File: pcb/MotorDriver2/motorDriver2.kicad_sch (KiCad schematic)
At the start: 22 parts, among them Q1 IRLZ44NSTRLPBF, Q6 IRLZ44NSTRLPBF, Q7 IRLZ44NSTRLPBF, Q8 IRLZ44NSTRLPBF

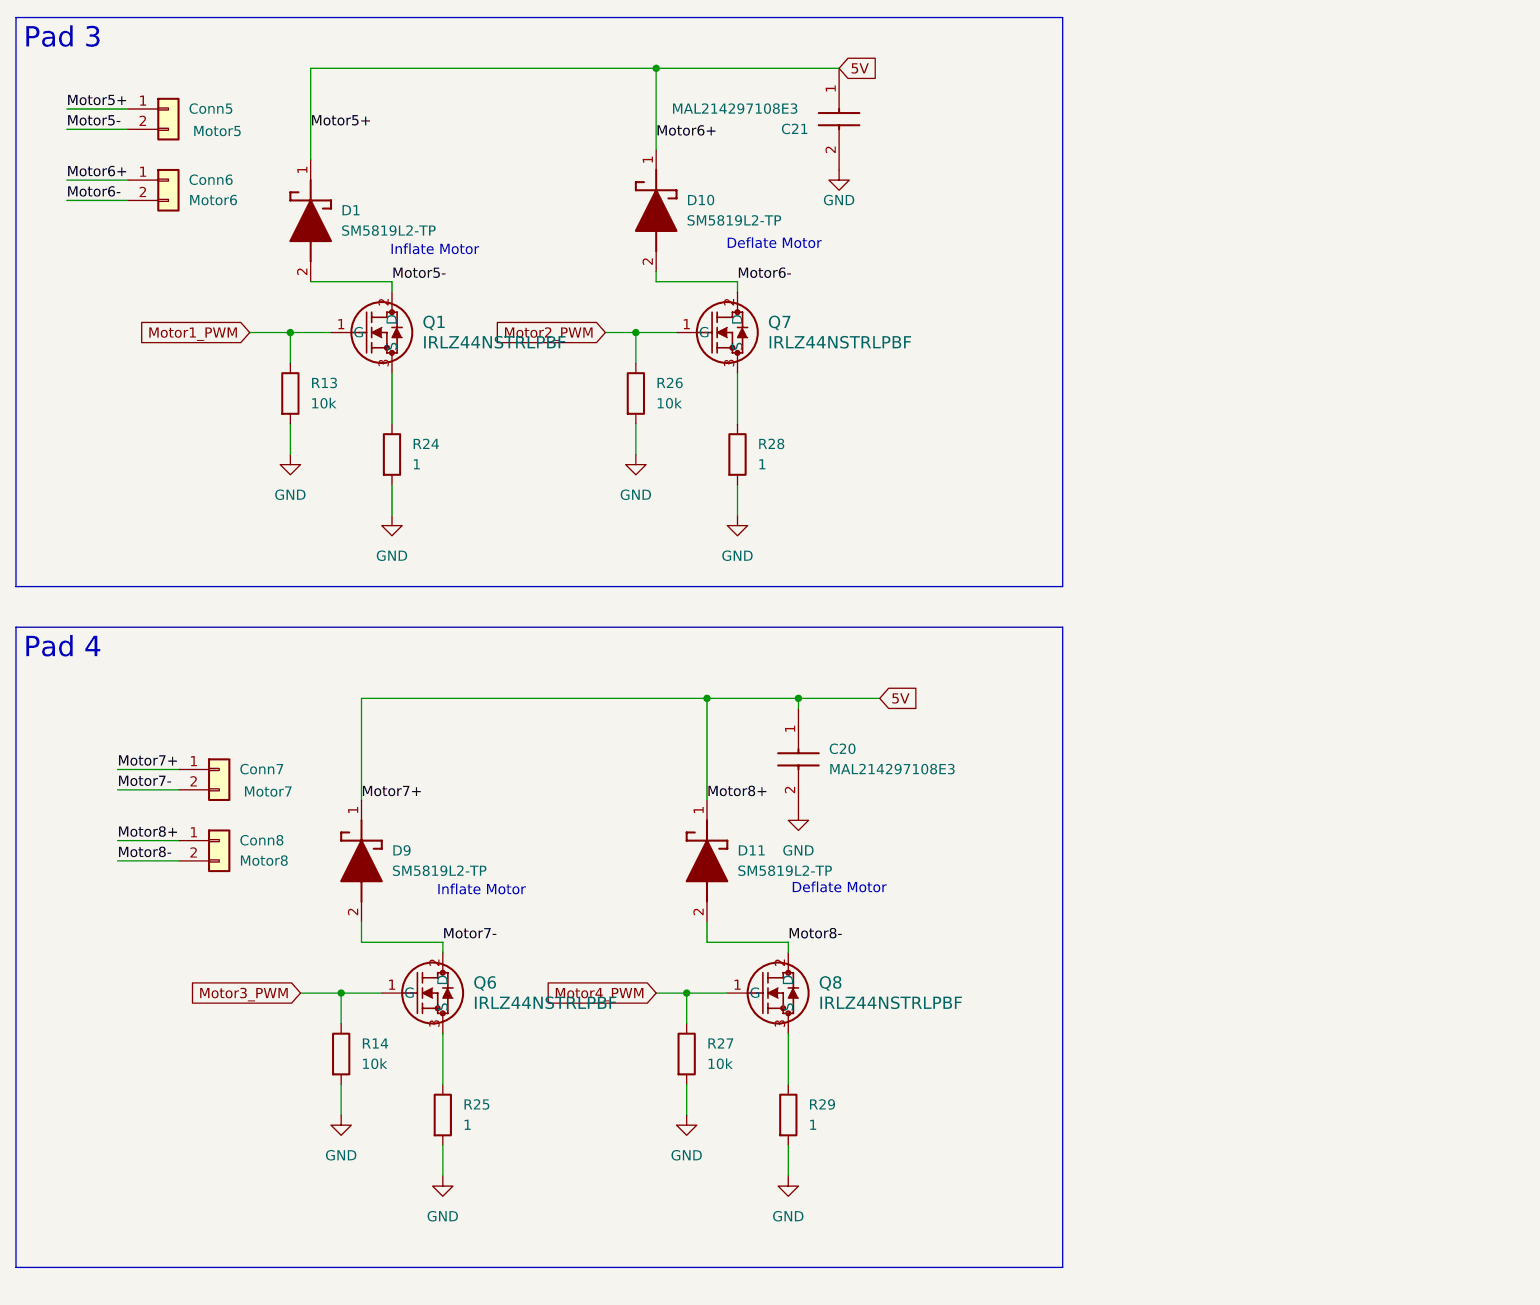
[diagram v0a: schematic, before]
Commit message: Modifying usb uart schematic
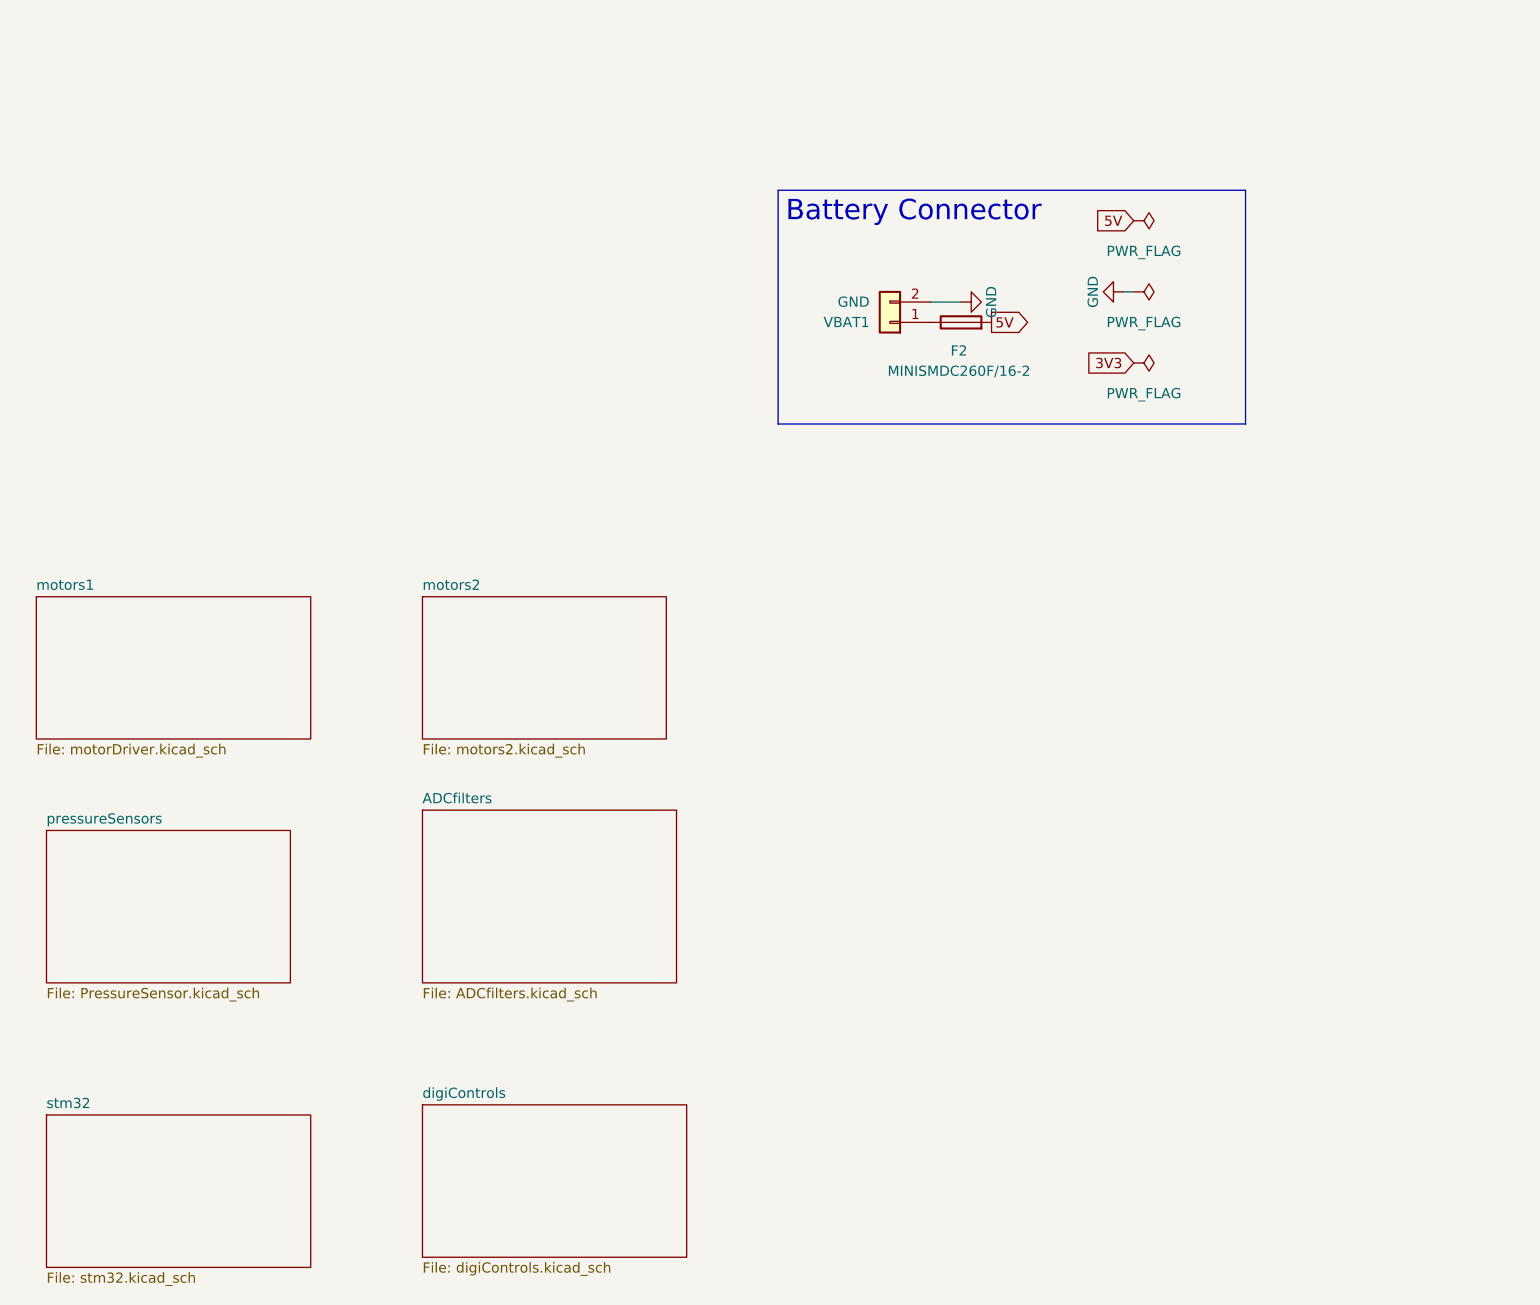
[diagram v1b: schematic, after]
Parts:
- removed C20, C21: MAL214297108E3, footprintLib:CAPAE680X800N, symbol pcb:MAL214297108E3
- removed Conn5: Motor5, Connector_PinHeader_2.54mm:PinHeader_1x02_P2.54mm_Vertical, symbol Connector_Generic:Conn_01x02
- removed Conn6: Motor6, Connector_PinHeader_2.54mm:PinHeader_1x02_P2.54mm_Vertical, symbol Connector_Generic:Conn_01x02
- removed Conn7: Motor7, Connector_PinHeader_2.54mm:PinHeader_1x02_P2.54mm_Vertical, symbol Connector_Generic:Conn_01x02
- removed Conn8: Motor8, Connector_PinHeader_2.54mm:PinHeader_1x02_P2.54mm_Vertical, symbol Connector_Generic:Conn_01x02
- removed D1, D10, D11, D9: SM5819L2-TP, footprintLib:SDO_SM5819L2-TP_MCE, symbol pcb:SM5819L2-TP
- removed Q1, Q6, Q7, Q8: IRLZ44NSTRLPBF, footprintLib:NMOSGDS_D2PAK_INF, symbol pcb:IRLZ44NSTRLPBF
- removed R13, R14, R26, R27: 10k, Resistor_SMD:R_0402_1005Metric, symbol Device:R
- removed R24, R25, R28, R29: 1, Resistor_SMD:R_1206_3216Metric, symbol Device:R
- added F2: MINISMDC260F/16-2, Fuse:Fuse_1812_4532Metric, symbol Device:Fuse
- added VBAT1: GND, Connector_PinHeader_2.54mm:PinHeader_1x02_P2.54mm_Vertical, symbol Connector_Generic:Conn_01x02
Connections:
- net 5V: now also F2.2
- net GND: now also VBAT1.2 (Pin_2)
- new net: F2.1, VBAT1.1 (Pin_1)
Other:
- added sheet ADCfilters (ADCfilters.kicad_sch)
- added sheet digiControls (digiControls.kicad_sch)
- added sheet motors1 (motorDriver.kicad_sch)
- added sheet motors2 (motors2.kicad_sch)
- added sheet pressureSensors (PressureSensor.kicad_sch)
- added sheet stm32 (stm32.kicad_sch)
- note removed: "Deflate Motor"
- note removed: "Inflate Motor"

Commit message: added ideal diode protection
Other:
- moved on the sheet: F2, VBAT1
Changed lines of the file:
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@@
 	(text_box "Battery Connector"
 		(exclude_from_sim no)
-		(at 124.46 48.26 0)
+		(at 130.81 101.6 0)
 		(size 58.42 29.21)
 		(margins 0.9525 0.9525 0.9525 0.9525)
@@
 	(wire
 		(pts
-			(xy 147.32 62.23) (xy 143.51 62.23)
+			(xy 153.67 115.57) (xy 149.86 115.57)
 		)
 		(stroke
@@
 	(wire
 		(pts
-			(xy 167.64 60.96) (xy 168.91 60.96)
+			(xy 173.99 114.3) (xy 175.26 114.3)
 		)
 		(stroke
@@
 	(global_label "5V"
 		(shape input)
-		(at 168.91 52.07 180)
+		(at 175.26 105.41 180)
 		(fields_autoplaced yes)
 		(effects
@@
 		)
 		(property "Intersheetrefs" "${INTERSHEET_REFS}"
-			(at 163.6267 52.07 0)
+			(at 169.9767 105.41 0)
 			(effects
 				(font
@@
 	(global_label "3V3"
 		(shape input)
-		(at 168.91 69.85 180)
+		(at 175.26 123.19 180)
 		(fields_autoplaced yes)
 		(effects
@@
 		)
 		(property "Intersheetrefs" "${INTERSHEET_REFS}"
-			(at 162.4172 69.85 0)
+			(at 168.7672 123.19 0)
 			(effects
 				(font
@@
 	(global_label "5V"
 		(shape output)
-		(at 151.13 64.77 0)
+		(at 157.48 118.11 0)
 		(fields_autoplaced yes)
 		(effects
@@
 		)
 		(property "Intersheetrefs" "${INTERSHEET_REFS}"
-			(at 156.4133 64.77 0)
+			(at 162.7633 118.11 0)
 			(effects
 				(font
@@
 	(symbol
 		(lib_id "power:GND")
-		(at 167.64 60.96 270)
+		(at 173.99 114.3 270)
 		(unit 1)
 		(exclude_from_sim no)
@@
 		(dnp no)
 		(property "Reference" "#PWR012"
-			(at 161.29 60.96 0)
+			(at 167.64 114.3 0)
 			(effects
 				(font
@@
 		)
 		(property "Value" "GND"
-			(at 163.83 60.96 0)
+			(at 170.18 114.3 0)
 			(effects
 				(font
@@
 		)
 		(property "Footprint" ""
-			(at 167.64 60.96 0)
+			(at 173.99 114.3 0)
 			(effects
 				(font
@@
 		)
 		(property "Datasheet" ""
-			(at 167.64 60.96 0)
+			(at 173.99 114.3 0)
 			(effects
 				(font
@@
 		)
 		(property "Description" "Power symbol creates a global label with name \"GND\" , ground"
-			(at 167.64 60.96 0)
+			(at 173.99 114.3 0)
 			(effects
 				(font
@@
 	(symbol
 		(lib_id "power:PWR_FLAG")
-		(at 168.91 52.07 270)
+		(at 175.26 105.41 270)
 		(unit 1)
 		(exclude_from_sim no)
@@
 		(fields_autoplaced yes)
 		(property "Reference" "#FLG01"
-			(at 170.815 52.07 0)
+			(at 177.165 105.41 0)
 			(effects
 				(font
@@
 		)
 		(property "Value" "PWR_FLAG"
-			(at 170.18 55.88 90)
+			(at 176.53 109.22 90)
 			(effects
 				(font
@@
 		)
 		(property "Footprint" ""
-			(at 168.91 52.07 0)
+			(at 175.26 105.41 0)
 			(effects
 				(font
@@
 		)
 		(property "Datasheet" "~"
-			(at 168.91 52.07 0)
+			(at 175.26 105.41 0)
 			(effects
 				(font
@@
 		)
 		(property "Description" "Special symbol for telling ERC where power comes from"
-			(at 168.91 52.07 0)
+			(at 175.26 105.41 0)
 			(effects
 				(font
@@
 	(symbol
 		(lib_id "Connector_Generic:Conn_01x02")
-		(at 138.43 64.77 180)
+		(at 144.78 118.11 180)
 		(unit 1)
 		(exclude_from_sim no)
@@
 		(dnp no)
 		(property "Reference" "VBAT1"
-			(at 135.89 64.77 0)
+			(at 142.24 118.11 0)
 			(effects
 				(font
@@
 		)
 		(property "Value" "GND"
-			(at 135.89 62.2301 0)
+			(at 142.24 115.5701 0)
 			(effects
 				(font
@@
 		)
 		(property "Footprint" "Connector_PinHeader_2.54mm:PinHeader_1x02_P2.54mm_Vertical"
-			(at 138.43 64.77 0)
+			(at 144.78 118.11 0)
 			(effects
 				(font
@@
 		)
 		(property "Datasheet" "~"
-			(at 138.43 64.77 0)
+			(at 144.78 118.11 0)
 			(effects
 				(font
@@
 		)
 		(property "Description" "Generic connector, single row, 01x02, script generated (kicad-library-utils/schlib/autogen/connector/)"
-			(at 138.43 64.77 0)
+			(at 144.78 118.11 0)
 			(effects
 				(font
@@
 	(symbol
 		(lib_id "power:GND")
-		(at 147.32 62.23 90)
+		(at 153.67 115.57 90)
 		(unit 1)
 		(exclude_from_sim no)
@@
 		(dnp no)
 		(property "Reference" "#PWR011"
-			(at 153.67 62.23 0)
+			(at 160.02 115.57 0)
 			(effects
 				(font
@@
 		)
 		(property "Value" "GND"
-			(at 151.13 62.23 0)
+			(at 157.48 115.57 0)
 			(effects
 				(font
@@
 		)
 		(property "Footprint" ""
-			(at 147.32 62.23 0)
+			(at 153.67 115.57 0)
 			(effects
 				(font
@@
 		)
 		(property "Datasheet" ""
-			(at 147.32 62.23 0)
+			(at 153.67 115.57 0)
 			(effects
 				(font
@@
 		)
 		(property "Description" "Power symbol creates a global label with name \"GND\" , ground"
-			(at 147.32 62.23 0)
+			(at 153.67 115.57 0)
 			(effects
 				(font
@@
 	(symbol
 		(lib_id "power:PWR_FLAG")
-		(at 168.91 69.85 270)
+		(at 175.26 123.19 270)
 		(unit 1)
 		(exclude_from_sim no)
@@
 		(fields_autoplaced yes)
 		(property "Reference" "#FLG03"
-			(at 170.815 69.85 0)
+			(at 177.165 123.19 0)
 			(effects
 				(font
@@
 		)
 		(property "Value" "PWR_FLAG"
-			(at 170.18 73.66 90)
+			(at 176.53 127 90)
 			(effects
 				(font
@@
 		)
 		(property "Footprint" ""
-			(at 168.91 69.85 0)
+			(at 175.26 123.19 0)
 			(effects
 				(font
@@
 		)
 		(property "Datasheet" "~"
-			(at 168.91 69.85 0)
+			(at 175.26 123.19 0)
 			(effects
 				(font
@@
 		)
 		(property "Description" "Special symbol for telling ERC where power comes from"
-			(at 168.91 69.85 0)
+			(at 175.26 123.19 0)
 			(effects
 				(font
@@
 	(symbol
 		(lib_id "power:PWR_FLAG")
-		(at 168.91 60.96 270)
+		(at 175.26 114.3 270)
 		(unit 1)
 		(exclude_from_sim no)
@@
 		(fields_autoplaced yes)
 		(property "Reference" "#FLG02"
-			(at 170.815 60.96 0)
+			(at 177.165 114.3 0)
 			(effects
 				(font
@@
 		)
 		(property "Value" "PWR_FLAG"
-			(at 170.18 64.77 90)
+			(at 176.53 118.11 90)
 			(effects
 				(font
@@
 		)
 		(property "Footprint" ""
-			(at 168.91 60.96 0)
+			(at 175.26 114.3 0)
 			(effects
 				(font
@@
 		)
 		(property "Datasheet" "~"
-			(at 168.91 60.96 0)
+			(at 175.26 114.3 0)
 			(effects
 				(font
@@
 		)
 		(property "Description" "Special symbol for telling ERC where power comes from"
-			(at 168.91 60.96 0)
+			(at 175.26 114.3 0)
 			(effects
 				(font
@@
 	(symbol
 		(lib_id "Device:Fuse")
-		(at 147.32 64.77 90)
+		(at 153.67 118.11 90)
 		(unit 1)
 		(exclude_from_sim no)
@@
 		(dnp no)
 		(property "Reference" "F2"
-			(at 147.066 68.326 90)
+			(at 153.416 121.666 90)
 			(effects
 				(font
@@
 		)
 		(property "Value" "MINISMDC260F/16-2"
-			(at 147.066 70.866 90)
+			(at 153.416 124.206 90)
 			(effects
 				(font
@@
 		)
 		(property "Footprint" "Fuse:Fuse_1812_4532Metric"
-			(at 147.32 66.548 90)
+			(at 153.67 119.888 90)
 			(effects
 				(font
@@
 		)
 		(property "Datasheet" "~"
-			(at 147.32 64.77 0)
+			(at 153.67 118.11 0)
 			(effects
 				(font
@@
 		)
 		(property "Description" "Fuse"
-			(at 147.32 64.77 0)
-			(effects
-				(font
+			(at 153.67 118.11 0)
+			(effects
+				(font

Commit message: Laying out PCB
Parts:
- F2: LCSC (none) -> C16490
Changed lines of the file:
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@@
 		(on_board yes)
 		(dnp no)
-		(property "Reference" "#PWR012"
+		(property "Reference" "#PWR02"
 			(at 167.64 114.3 0)
 			(effects
@@
 			(project "MotorDriver2"
 				(path "/6e0510ec-6dbc-4bc1-a315-3680b1127a92"
-					(reference "#PWR012")
+					(reference "#PWR02")
 					(unit 1)
 				)
@@
 		(on_board yes)
 		(dnp no)
-		(property "Reference" "#PWR011"
+		(property "Reference" "#PWR01"
 			(at 160.02 115.57 0)
 			(effects
@@
 			(project "MotorDriver2"
 				(path "/6e0510ec-6dbc-4bc1-a315-3680b1127a92"
-					(reference "#PWR011")
+					(reference "#PWR01")
 					(unit 1)
 				)
@@
 			(at 153.67 118.11 0)
 			(effects
+				(font
+					(size 1.27 1.27)
+				)
+				(hide yes)
+			)
+		)
+		(property "LCSC" "C16490"
+			(at 153.67 118.11 0)
+			(effects

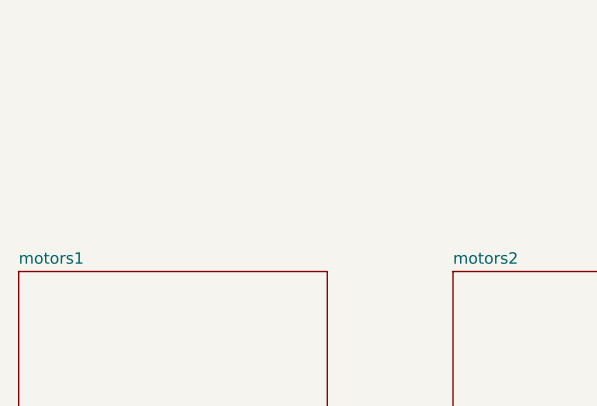
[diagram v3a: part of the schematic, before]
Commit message: Added STLink Connector
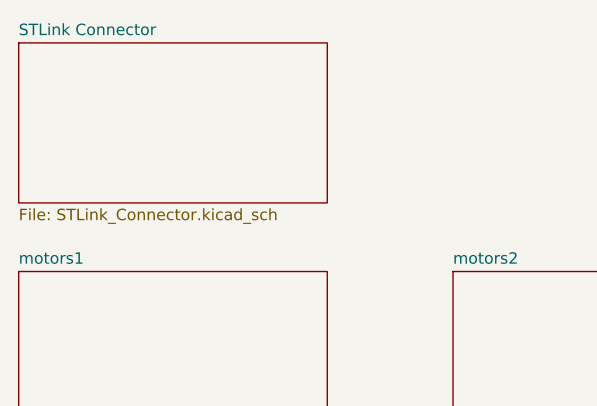
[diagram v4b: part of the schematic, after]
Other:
- added sheet STLink Connector (STLink_Connector.kicad_sch)
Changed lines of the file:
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@@
 		)
 		(instances
-			(project "MotorDriver2"
+			(project "motorDriver2"
 				(path "/6e0510ec-6dbc-4bc1-a315-3680b1127a92"
 					(page "6")
@@
 		)
 		(instances
-			(project "MotorDriver2"
+			(project "motorDriver2"
 				(path "/6e0510ec-6dbc-4bc1-a315-3680b1127a92"
 					(page "7")
+				)
+			)
+		)
+	)
+	(sheet
+		(at 31.75 73.66)
+		(size 34.29 17.78)
+		(exclude_from_sim no)
+		(in_bom yes)
+		(on_board yes)
+		(dnp no)
+		(fields_autoplaced yes)
+		(stroke
+			(width 0.1524)
+			(type solid)
+		)
+		(fill
+			(color 0 0 0 0.0000)
+		)
+		(property "Sheetname" "STLink Connector"
+			(at 31.75 72.9484 0)
+			(effects
+				(font
+					(size 1.27 1.27)
+				)
+				(justify left bottom)
+			)
+		)
+		(property "Sheetfile" "STLink_Connector.kicad_sch"
+			(at 31.75 92.0246 0)
+			(effects
+				(font
+					(size 1.27 1.27)
+				)
+				(justify left top)
+			)
+		)
+		(instances
+			(project "motorDriver2"
+				(path "/6e0510ec-6dbc-4bc1-a315-3680b1127a92"
+					(page "8")
 				)
 			)
@@
 		)
 		(instances
-			(project "MotorDriver2"
+			(project "motorDriver2"
 				(path "/6e0510ec-6dbc-4bc1-a315-3680b1127a92"
 					(page "4")
@@
 		)
 		(instances
-			(project "MotorDriver2"
+			(project "motorDriver2"
 				(path "/6e0510ec-6dbc-4bc1-a315-3680b1127a92"
 					(page "5")
@@
 		)
 		(instances
-			(project "MotorDriver2"
+			(project "motorDriver2"
 				(path "/6e0510ec-6dbc-4bc1-a315-3680b1127a92"
 					(page "3")
@@
 		)
 		(instances
-			(project "MotorDriver2"
+			(project "motorDriver2"
 				(path "/6e0510ec-6dbc-4bc1-a315-3680b1127a92"
 					(page "2")
